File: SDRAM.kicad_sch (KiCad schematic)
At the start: 27 parts, among them J1 Micro_SD_Card_Det_Hirose_DM3AT, U1 MT25Q, U11 MT48LC16M16A2P, U7 CAT24C128

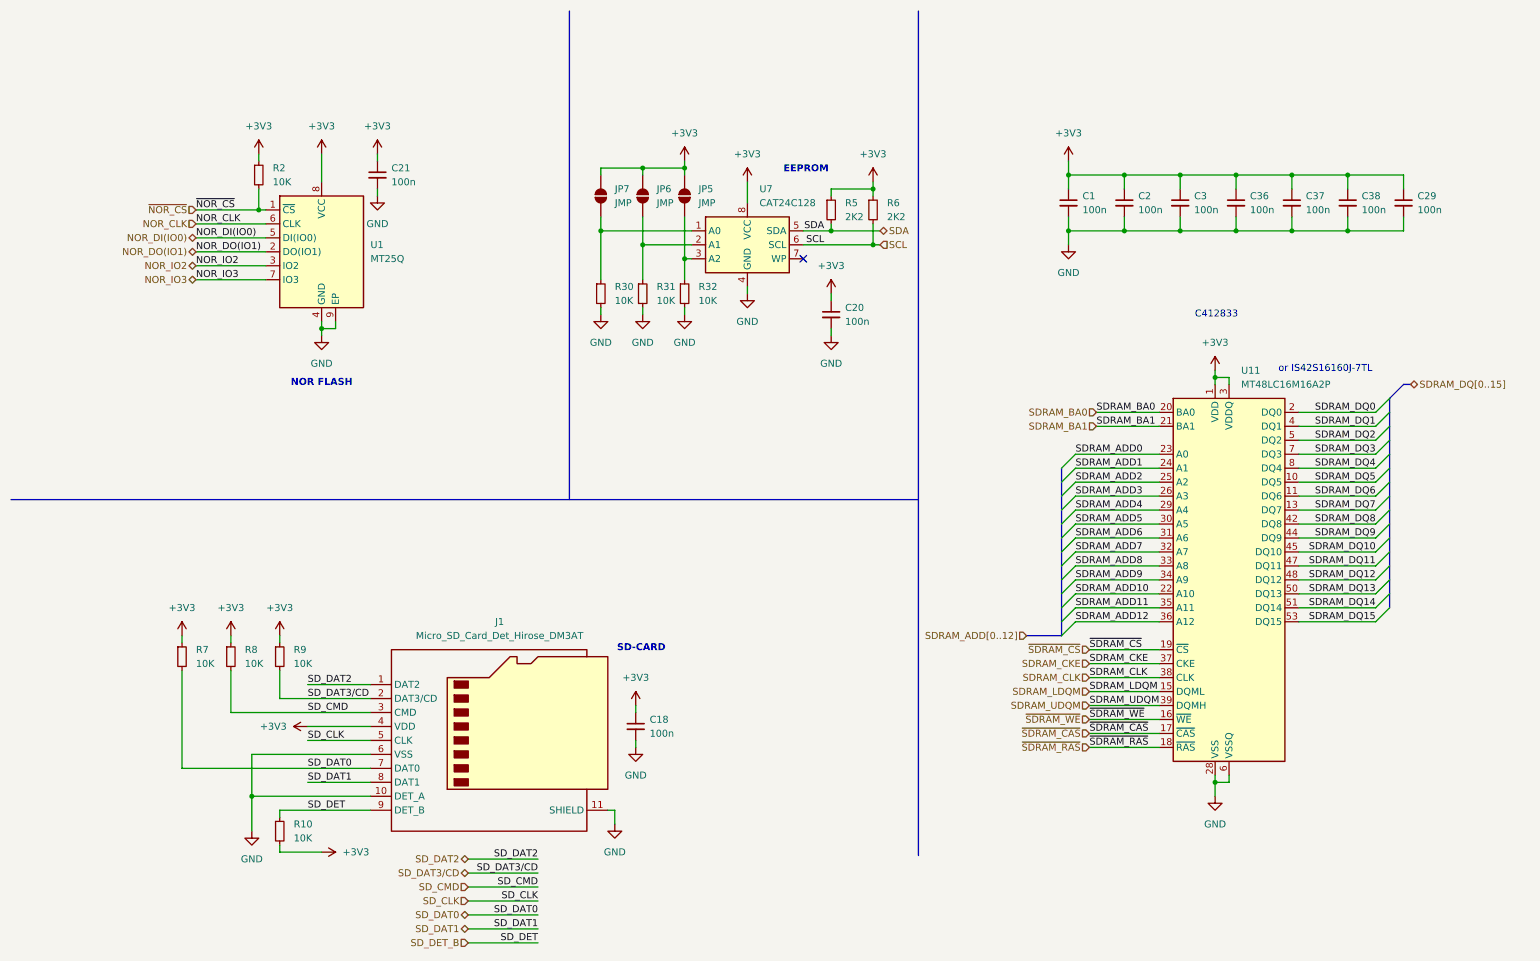
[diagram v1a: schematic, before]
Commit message: Cleaning schematic, added more independently schematics
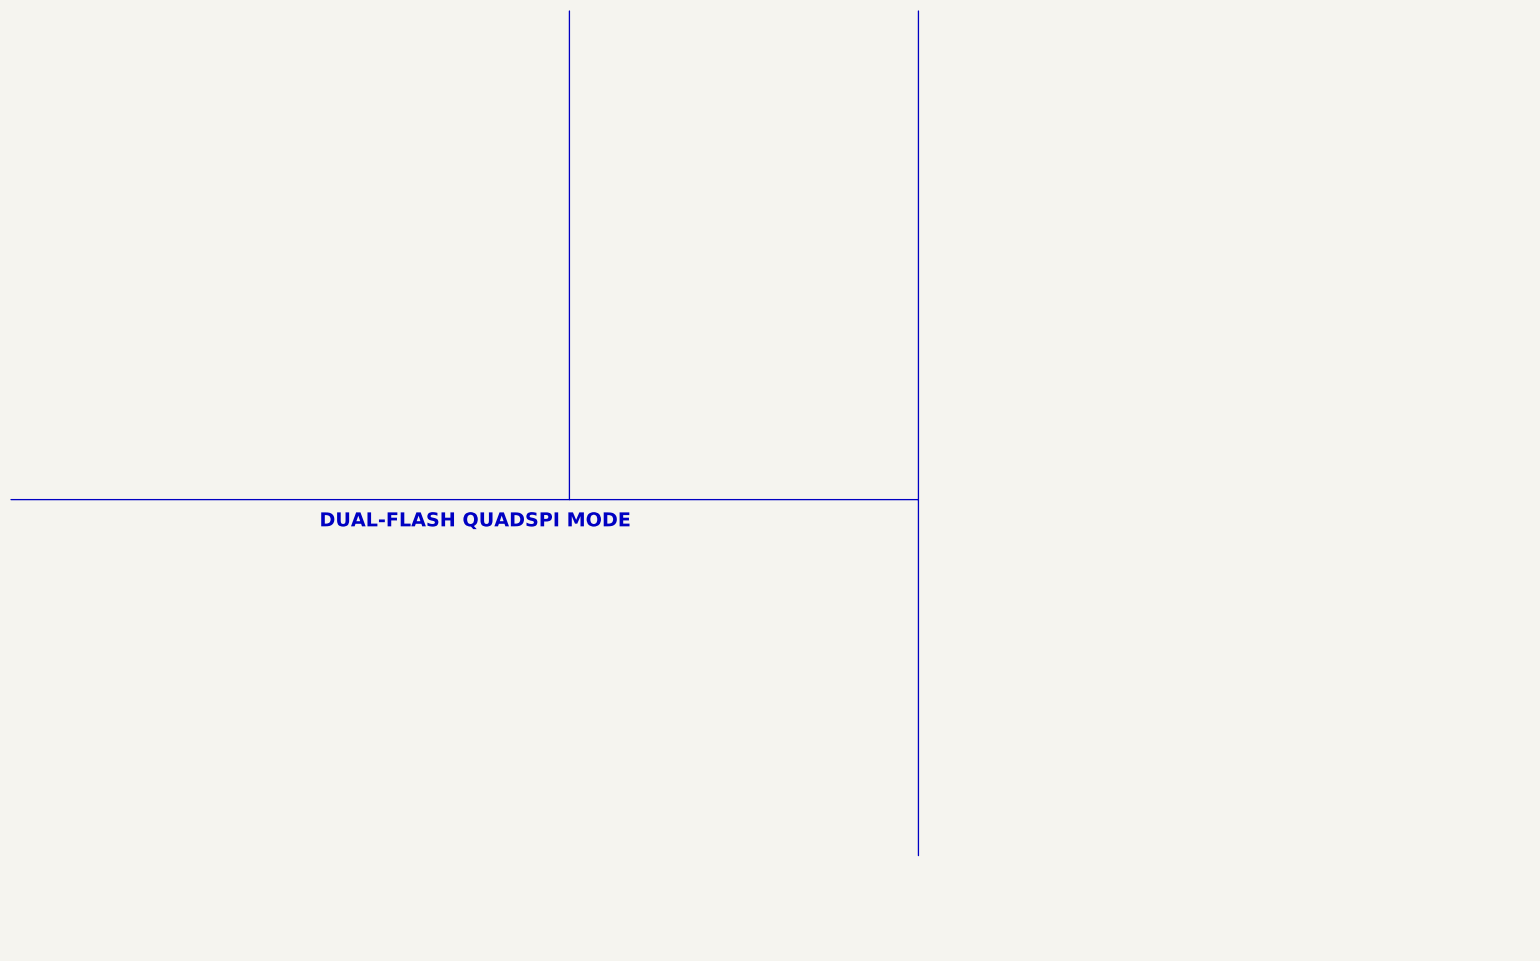
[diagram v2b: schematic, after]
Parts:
- removed C1, C18, C2, C20, C21, C29, C3, C36, C37, C38: 100n, Capacitor_SMD:C_0402_1005Metric, symbol Device:C_Small
- removed J1: Micro_SD_Card_Det_Hirose_DM3AT, Connector_Card:microSD_HC_Hirose_DM3AT-SF-PEJM5, symbol Connector:Micro_SD_Card_Det_Hirose_DM3AT
- removed JP5, JP6, JP7: JMP, Jumper:SolderJumper-2_P1.3mm_Open_RoundedPad1.0x1.5mm, symbol Jumper:SolderJumper_2_Open
- removed R10, R2, R30, R31, R32, R7, R8, R9: 10K, Resistor_SMD:R_0402_1005Metric, symbol Device:R_Small
- removed R5, R6: 2K2, Resistor_SMD:R_0402_1005Metric, symbol Device:R_Small
- removed U1: MT25Q, Package_SON:WSON-8-1EP_8x6mm_P1.27mm_EP3.4x4.3mm, symbol Memory_Flash:W25Q32JVZP
- removed U11: MT48LC16M16A2P, Package_SO:TSOP-II-54_22.2x10.16mm_P0.8mm, symbol Memory_RAM:MT48LC16M16A2P
- removed U7: CAT24C128, Package_SO:SOIC-8_3.9x4.9mm_P1.27mm, symbol Memory_EEPROM:CAT24C128
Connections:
- no-connect marks 1 -> 0
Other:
- note added: "DUAL-FLASH QUADSPI MODE"
- note removed: "C412833"
- note removed: "EEPROM"
- note removed: "NOR FLASH"
- note removed: "SD-CARD"
- note removed: "or IS42S16160J-7TL"
